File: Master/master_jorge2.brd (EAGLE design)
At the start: 44.7 x 35.8 mm, 51 parts, among them J1 ISP, K1 653002114822, K2 653002114822, K3 653002114822, K4 653002114822, U1 ATMEGA128RFA1, U2 TPS73633-DBVT, U3 ULN2003ADR, U4 LSM303D, U5 L3GD20H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

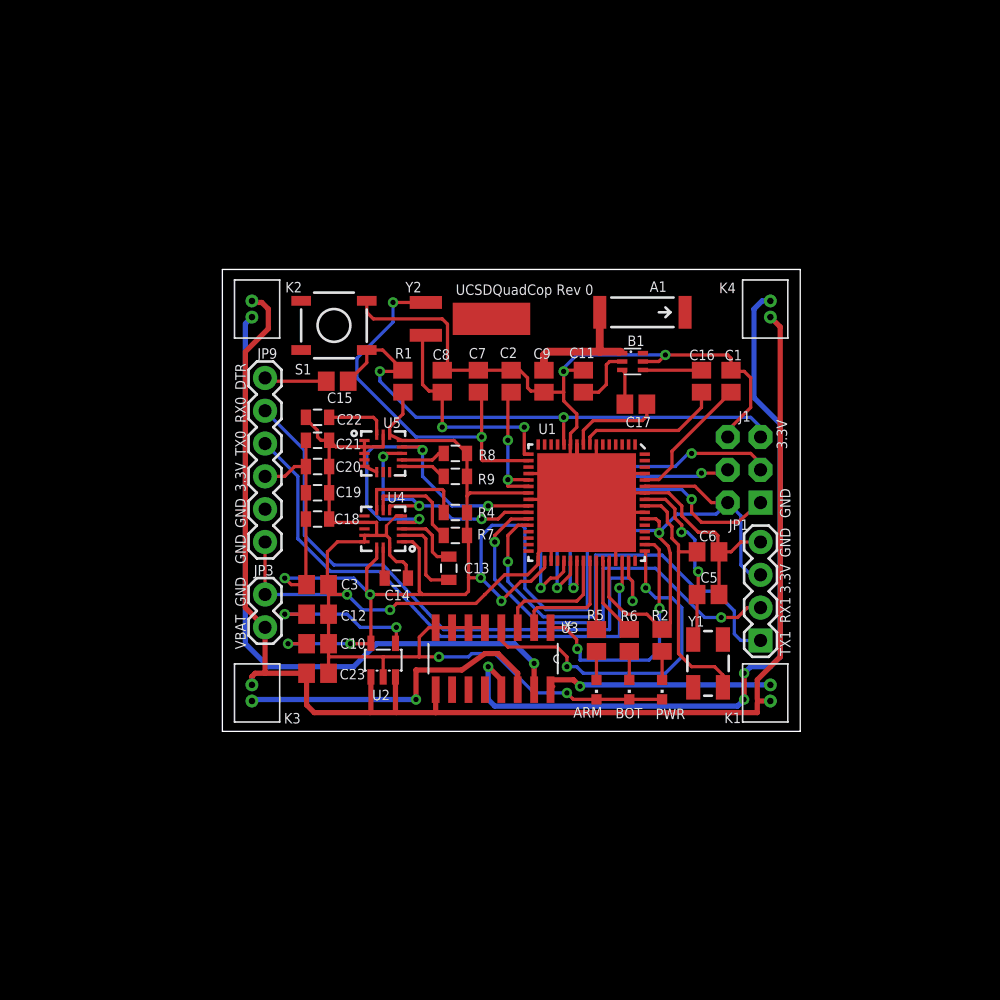
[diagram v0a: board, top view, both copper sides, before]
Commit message: Adding New schematic/board
Adding new schematic and board. The new board contains a different
border line  for placing the motors directly in the pcb.
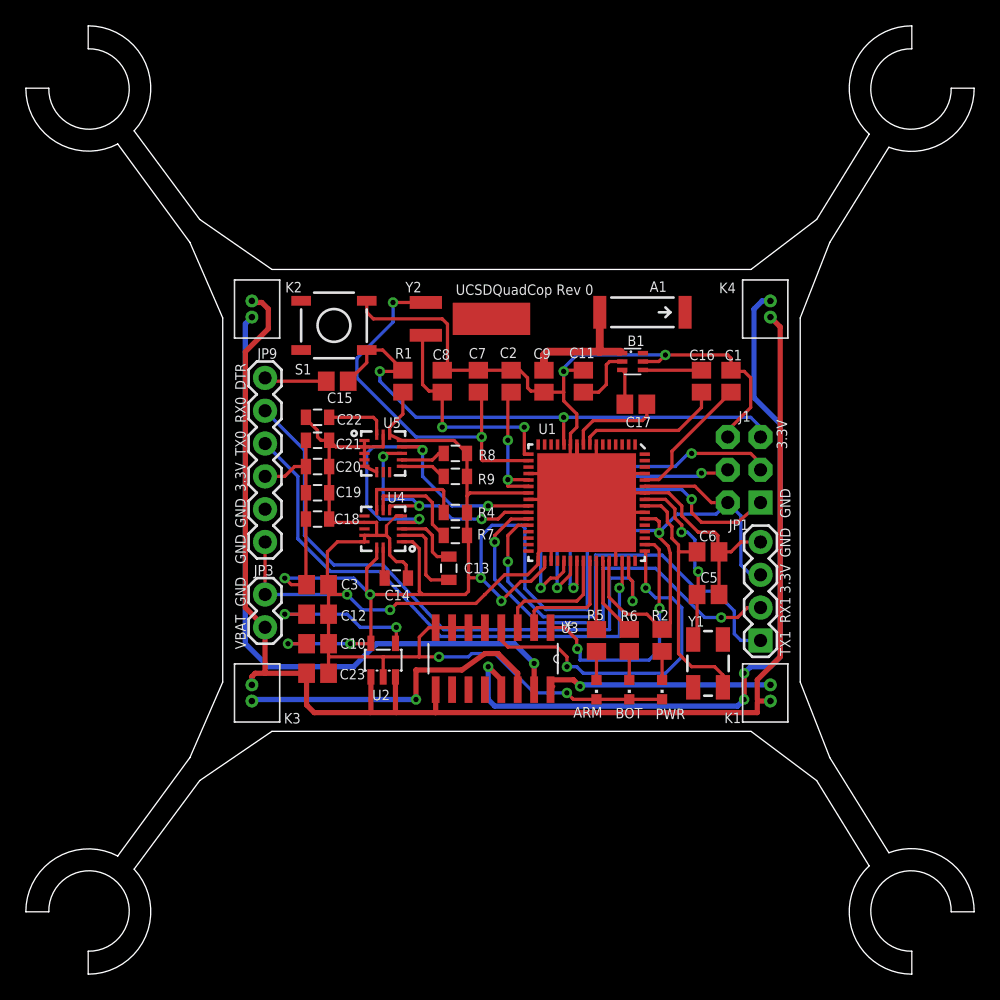
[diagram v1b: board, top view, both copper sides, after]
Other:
- board size 44.7 x 35.8 mm -> 73.4 x 73.4 mm
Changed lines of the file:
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@@
 <setting verticaltext="up"/>
 </settings>
-<grid distance="0.01" unitdist="inch" unit="inch" style="lines" multiple="1" display="no" altdistance="0.025" altunitdist="inch" altunit="inch"/>
+<grid distance="0.01" unitdist="inch" unit="inch" style="lines" multiple="1" display="no" altdistance="0.01" altunitdist="inch" altunit="inch"/>
 <layers>
 <layer number="1" name="Top" color="4" fill="1" visible="yes" active="yes"/>
@@
 <layer number="35" name="tGlue" color="7" fill="4" visible="no" active="yes"/>
 <layer number="36" name="bGlue" color="7" fill="5" visible="no" active="yes"/>
-<layer number="37" name="tTest" color="7" fill="1" visible="no" active="yes"/>
+<layer number="37" name="tTest" color="7" fill="1" visible="yes" active="yes"/>
 <layer number="38" name="bTest" color="7" fill="1" visible="no" active="yes"/>
 <layer number="39" name="tKeepout" color="4" fill="11" visible="no" active="yes"/>
@@
 <layer number="111" name="LPC17xx" color="7" fill="1" visible="no" active="no"/>
 <layer number="112" name="tSilk" color="7" fill="1" visible="no" active="no"/>
-<layer number="113" name="IDFDebug" color="4" fill="1" visible="no" active="yes"/>
+<layer number="113" name="IDFDebug" color="4" fill="1" visible="yes" active="yes"/>
 <layer number="116" name="Patch_BOT" color="9" fill="4" visible="no" active="yes"/>
 <layer number="118" name="Rect_Pads" color="7" fill="1" visible="no" active="no"/>
@@
 <board>
 <plain>
-<wire x1="-0.0254" y1="0" x2="44.7042" y2="0" width="0" layer="20"/>
-<wire x1="44.7042" y1="0" x2="44.7042" y2="35.7532" width="0" layer="20"/>
-<wire x1="44.7042" y1="35.7532" x2="-0.0254" y2="35.7532" width="0" layer="20"/>
-<wire x1="-0.0254" y1="35.7532" x2="-0.0254" y2="0" width="0" layer="20"/>
 <polygon width="0.254" layer="41">
 <vertex x="24.3332" y="30.0482"/>
@@
 Revision Number: 0</text>
 <text x="18.034" y="33.782" size="0.8128" layer="21">UCSDQuadCop Rev 0</text>
+<wire x1="-13.462" y1="49.784" x2="-10.414" y2="52.832" width="0" layer="20" curve="272.385944"/>
+<wire x1="-6.858" y1="46.482" x2="-10.414" y2="54.61" width="0" layer="20" curve="132.878904"/>
+<wire x1="-8.128" y1="45.466" x2="-15.24" y2="49.784" width="0" layer="20" curve="-117.897271"/>
+<wire x1="53.34" y1="52.832" x2="56.388" y2="49.784" width="0" layer="20" curve="272.385944"/>
+<wire x1="56.388" y1="-13.97" x2="53.34" y2="-17.018" width="0" layer="20" curve="272.385944"/>
+<wire x1="-10.414" y1="-17.018" x2="-13.462" y2="-13.97" width="0" layer="20" curve="272.385944"/>
+<wire x1="-6.858" y1="-10.668" x2="-10.414" y2="-18.796" width="0" layer="20" curve="-132.878904"/>
+<wire x1="-8.128" y1="-9.652" x2="-15.24" y2="-13.97" width="0" layer="20" curve="117.897271"/>
+<wire x1="51.562" y1="-9.398" x2="58.166" y2="-13.97" width="0" layer="20" curve="-111.250506"/>
+<wire x1="50.038" y1="-10.414" x2="53.34" y2="-18.796" width="0" layer="20" curve="137.121096"/>
+<wire x1="51.562" y1="45.212" x2="58.166" y2="49.784" width="0" layer="20" curve="111.250506"/>
+<wire x1="50.038" y1="46.228" x2="53.34" y2="54.61" width="0" layer="20" curve="-137.121096"/>
+<wire x1="-6.858" y1="-10.668" x2="-1.778" y2="-3.81" width="0" layer="20"/>
+<wire x1="-1.778" y1="-3.81" x2="3.81" y2="0" width="0" layer="20"/>
+<wire x1="3.81" y1="0" x2="40.894" y2="0" width="0" layer="20"/>
+<wire x1="40.894" y1="0" x2="45.974" y2="-3.81" width="0" layer="20"/>
+<wire x1="45.974" y1="-3.81" x2="50.038" y2="-10.414" width="0" layer="20"/>
+<wire x1="51.562" y1="-9.398" x2="46.99" y2="-2.032" width="0" layer="20"/>
+<wire x1="46.99" y1="-2.032" x2="44.704" y2="3.81" width="0" layer="20"/>
+<wire x1="44.704" y1="3.81" x2="44.704" y2="32.004" width="0" layer="20"/>
+<wire x1="44.704" y1="32.004" x2="46.99" y2="37.846" width="0" layer="20"/>
+<wire x1="46.99" y1="37.846" x2="51.562" y2="45.212" width="0" layer="20"/>
+<wire x1="50.038" y1="46.228" x2="45.974" y2="39.624" width="0" layer="20"/>
+<wire x1="-8.128" y1="-9.652" x2="-2.54" y2="-2.032" width="0" layer="20"/>
+<wire x1="-2.54" y1="-2.032" x2="0" y2="3.81" width="0" layer="20"/>
+<wire x1="0" y1="3.81" x2="0" y2="32.004" width="0" layer="20"/>
+<wire x1="0" y1="32.004" x2="-2.54" y2="37.846" width="0" layer="20"/>
+<wire x1="-2.54" y1="37.846" x2="-8.128" y2="45.466" width="0" layer="20"/>
+<wire x1="-6.858" y1="46.482" x2="-1.778" y2="39.624" width="0" layer="20"/>
+<wire x1="-1.778" y1="39.624" x2="3.81" y2="35.753040625" width="0" layer="20"/>
+<wire x1="3.81" y1="35.753040625" x2="40.894" y2="35.753040625" width="0" layer="20"/>
+<wire x1="40.894" y1="35.753040625" x2="45.974" y2="39.624" width="0" layer="20"/>
+<wire x1="53.34" y1="54.61" x2="53.34" y2="52.832" width="0" layer="20"/>
+<wire x1="58.166" y1="49.784" x2="56.388" y2="49.784" width="0" layer="20"/>
+<wire x1="58.166" y1="-13.97" x2="56.388" y2="-13.97" width="0" layer="20"/>
+<wire x1="53.34" y1="-18.796" x2="53.34" y2="-17.018" width="0" layer="20"/>
+<wire x1="-10.414" y1="-18.796" x2="-10.414" y2="-17.018" width="0" layer="20"/>
+<wire x1="-15.24" y1="-13.97" x2="-13.462" y2="-13.97" width="0" layer="20"/>
+<wire x1="-10.414" y1="54.61" x2="-10.414" y2="52.832" width="0" layer="20"/>
+<wire x1="-13.462" y1="49.784" x2="-15.24" y2="49.784" width="0" layer="20"/>
 </plain>
 <attributes>
